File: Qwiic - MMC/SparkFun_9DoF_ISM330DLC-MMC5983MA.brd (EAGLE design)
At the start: 25.4 x 25.4 mm, 69 parts, among them J1 QWIIC_RIGHT_ANGLE, J2 QWIIC_RIGHT_ANGLE, U1 ISM330DLC, U2 MMC5983MA_QFN16

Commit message: Updates silk on board to reflect part change
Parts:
- removed U$31: (no value), top:ISM330DHCX5984
- added U$12: (no value), top:ISM330DLC5984
- U$10: device top:#ACC_SCL#8 -> top:#AUX_SCL#8
- U$11: device top:#ACC_SDA#7 -> top:#AUX_SDA#7
- U$23: device top:ISM330DHCX5984 -> top:ISM330DLC5984
- moved U$23 7.37 mm to (5.71, 13.0), flipped to the bottom, turned to 270 degrees
- moved U$11 0.13 mm to (16.5, 19.7)
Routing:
- net GND: vias 25 -> 24
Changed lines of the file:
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@@
 <attribute name="VALUE" x="8.89" y="17.018" size="0.6096" layer="27" font="vector" ratio="20" rot="R270" align="top-center"/>
 </element>
-<element name="U$10" library="top" package="#ACC_SCL#8" value="" x="13.97" y="19.812" smashed="yes" rot="MR270"/>
-<element name="U$11" library="top" package="#ACC_SDA#7" value="" x="16.637" y="19.685" smashed="yes" rot="MR270"/>
 <element name="U$19" library="top" package="#ASDA#9" value="" x="16.637" y="20.955" smashed="yes" rot="R90"/>
 <element name="U$20" library="top" package="#ASCL#10" value="" x="13.97" y="21.336" smashed="yes" rot="R90"/>
 <element name="U$21" library="top" package="MMC5983MA24" value="" x="6.985" y="20.32" smashed="yes" rot="R90"/>
-<element name="U$23" library="top" package="ISM330DHCX5984" value="" x="5.588" y="20.32" smashed="yes" rot="R90"/>
 <element name="U$24" library="top" package="9DOF24" value="" x="3.81" y="18.669" smashed="yes" rot="R90"/>
 <element name="U$30" library="top" package="9DOF24" value="" x="4.191" y="12.954" smashed="yes" rot="MR270"/>
-<element name="U$31" library="top" package="ISM330DHCX5984" value="" x="5.715" y="12.954" smashed="yes" rot="MR270"/>
 <element name="U$32" library="top" package="MMC5983MA24" value="" x="7.239" y="12.954" smashed="yes" rot="MR270"/>
 <element name="U$33" library="top" package="#0X6A#15" value="" x="22.987" y="7.239" smashed="yes" rot="MR0"/>
@@
 <element name="U$8" library="top" package="#MAG_INT#12" value="" x="8.89" y="19.812" smashed="yes" rot="MR270"/>
 <element name="U$9" library="top" package="#ACC_INT#11" value="" x="11.43" y="19.939" smashed="yes" rot="MR270"/>
+<element name="U$12" library="top" package="ISM330DLC5984" value="" x="5.461" y="19.812" smashed="yes" rot="R90"/>
+<element name="U$23" library="top" package="ISM330DLC5984" value="" x="5.715" y="12.954" smashed="yes" rot="MR270"/>
+<element name="U$10" library="top" package="#AUX_SCL#8" value="" x="13.97" y="19.812" smashed="yes" rot="MR270"/>
+<element name="U$11" library="top" package="#AUX_SDA#7" value="" x="16.51" y="19.685" smashed="yes" rot="MR270"/>
 </elements>
 <signals>
@@
 <via x="22.225" y="7.366" extent="1-16" drill="0.3048"/>
 <via x="6.604" y="14.224" extent="1-16" drill="0.3048"/>
-<via x="5.334" y="15.875" extent="1-16" drill="0.3048"/>
 <via x="19.3802" y="5.1308" extent="1-16" drill="0.3048"/>
 <via x="8.3058" y="7.1628" extent="1-16" drill="0.3048"/>
@@
 <via x="13.8938" y="5.8928" extent="1-16" drill="0.3048"/>
 <via x="14.6558" y="4.1148" extent="1-16" drill="0.3048"/>
-<wire x1="21.717" y1="19.685" x2="23.1775" y2="18.542" width="0" layer="19" extent="16-16"/>
-<wire x1="15.5702" y1="21.5138" x2="21.717" y2="19.685" width="0" layer="19" extent="1-1"/>
-<wire x1="14.1732" y1="21.6408" x2="15.5702" y2="21.5138" width="0" layer="19" extent="1-1"/>
-<wire x1="12.5222" y1="21.5138" x2="14.1732" y2="21.6408" width="0" layer="19" extent="1-1"/>
-<wire x1="10.795" y1="19.05" x2="12.5222" y2="21.5138" width="0" layer="19" extent="1-1"/>
-<wire x1="11.954" y1="15.385" x2="10.795" y2="19.05" width="0" layer="19" extent="1-1"/>
-<wire x1="12.954" y1="15.385" x2="11.954" y2="15.385" width="0" layer="19" extent="1-1"/>
-<wire x1="11.954" y1="14.328" x2="11.954" y2="15.385" width="0" layer="19" extent="1-1"/>
-<wire x1="10.287" y1="13.97" x2="11.596" y2="13.97" width="0" layer="19" extent="1-1"/>
-<wire x1="15.494" y1="14.263" x2="14.224" y2="14.732" width="0" layer="19" extent="1-1"/>
-<wire x1="15.494" y1="12.954" x2="15.494" y2="14.263" width="0" layer="19" extent="1-1"/>
-<wire x1="11.596" y1="12.446" x2="11.596" y2="13.97" width="0" layer="19" extent="1-1"/>
-<wire x1="10.287" y1="12.446" x2="11.596" y2="12.446" width="0" layer="19" extent="1-1"/>
-<wire x1="12.2" y1="10.906" x2="11.596" y2="12.446" width="0" layer="19" extent="1-1"/>
-<wire x1="12.7" y1="10.906" x2="12.2" y2="10.906" width="0" layer="19" extent="1-1"/>
-<wire x1="10.668" y1="8.509" x2="12.2" y2="10.906" width="0" layer="19" extent="1-1"/>
-<wire x1="9.652" y1="9.04965" x2="10.668" y2="8.509" width="0" layer="19" extent="1-1"/>
-<wire x1="8.3058" y1="7.1628" x2="9.652" y2="9.04965" width="0" layer="19" extent="1-1"/>
-<wire x1="7.7978" y1="5.8928" x2="8.3058" y2="7.1628" width="0" layer="19" extent="1-1"/>
-<wire x1="9.7536" y1="6.096" x2="8.3058" y2="7.1628" width="0" layer="19" extent="1-1"/>
-<wire x1="6.5278" y1="8.1788" x2="8.3058" y2="7.1628" width="0" layer="19" extent="1-1"/>
-<wire x1="10.4648" y1="2.9718" x2="9.7536" y2="6.096" width="0" layer="19" extent="1-1"/>
-<wire x1="12.2682" y1="2.5908" x2="10.4648" y2="2.9718" width="0" layer="19" extent="1-1"/>
-<wire x1="14.6558" y1="4.1148" x2="12.2682" y2="2.5908" width="0" layer="19" extent="1-1"/>
-<wire x1="13.8938" y1="5.8928" x2="14.6558" y2="4.1148" width="0" layer="19" extent="1-1"/>
-<wire x1="17.4752" y1="5.6388" x2="14.6558" y2="4.1148" width="0" layer="19" extent="1-1"/>
-<wire x1="19.3802" y1="5.1308" x2="17.4752" y2="5.6388" width="0" layer="19" extent="1-1"/>
-<wire x1="20.916" y1="7.366" x2="19.3802" y2="5.1308" width="0" layer="19" extent="1-1"/>
-<wire x1="22.225" y1="7.366" x2="20.916" y2="7.366" width="0" layer="19" extent="1-1"/>
-<wire x1="16.7132" y1="8.4328" x2="17.4752" y2="5.6388" width="0" layer="19" extent="1-1"/>
-<wire x1="20.447" y1="10.287" x2="20.916" y2="7.366" width="0" layer="19" extent="1-1"/>
-<wire x1="20.2946" y1="11.2" x2="20.447" y2="10.287" width="0" layer="19" extent="1-1"/>
-<wire x1="18.923" y1="11.176" x2="20.2946" y2="11.2" width="0" layer="19" extent="1-1"/>
-<wire x1="6.604" y1="14.224" x2="10.287" y2="13.97" width="0" layer="19" extent="1-1"/>
-<wire x1="5.08" y1="14.2" x2="6.604" y2="14.224" width="0" layer="19" extent="1-1"/>
-<wire x1="5.334" y1="15.875" x2="5.08" y2="14.2" width="0" layer="19" extent="1-1"/>
-<wire x1="6.35" y1="1.27" x2="10.4648" y2="2.9718" width="0" layer="19" extent="1-1"/>
 </signal>
 <signal name="SCL">
@@
 <wire x1="7.874" y1="11.811" x2="7.6835" y2="12.0015" width="0.4064" layer="1"/>
 <wire x1="7.6835" y1="12.0015" x2="7.6835" y2="12.7635" width="0.4064" layer="1"/>
-<wire x1="12.6116" y1="19.304" x2="12.954" y2="18.389" width="0" layer="19" extent="1-1"/>
-<wire x1="9.652" y1="10.74965" x2="9.779" y2="11.811" width="0" layer="19" extent="1-1"/>
-<wire x1="14.196" y1="16.127" x2="15.494" y2="15.963" width="0" layer="19" extent="1-1"/>
-<wire x1="8.1788" y1="10.74965" x2="9.652" y2="10.74965" width="0" layer="19" extent="1-1"/>
-<wire x1="13.2" y1="10.906" x2="13.296" y2="12.446" width="0" layer="19" extent="1-1"/>
-<wire x1="11.5375" y1="10.656" x2="13.2" y2="10.906" width="0" layer="19" extent="1-1"/>
 </signal>
 <signal name="N$5">

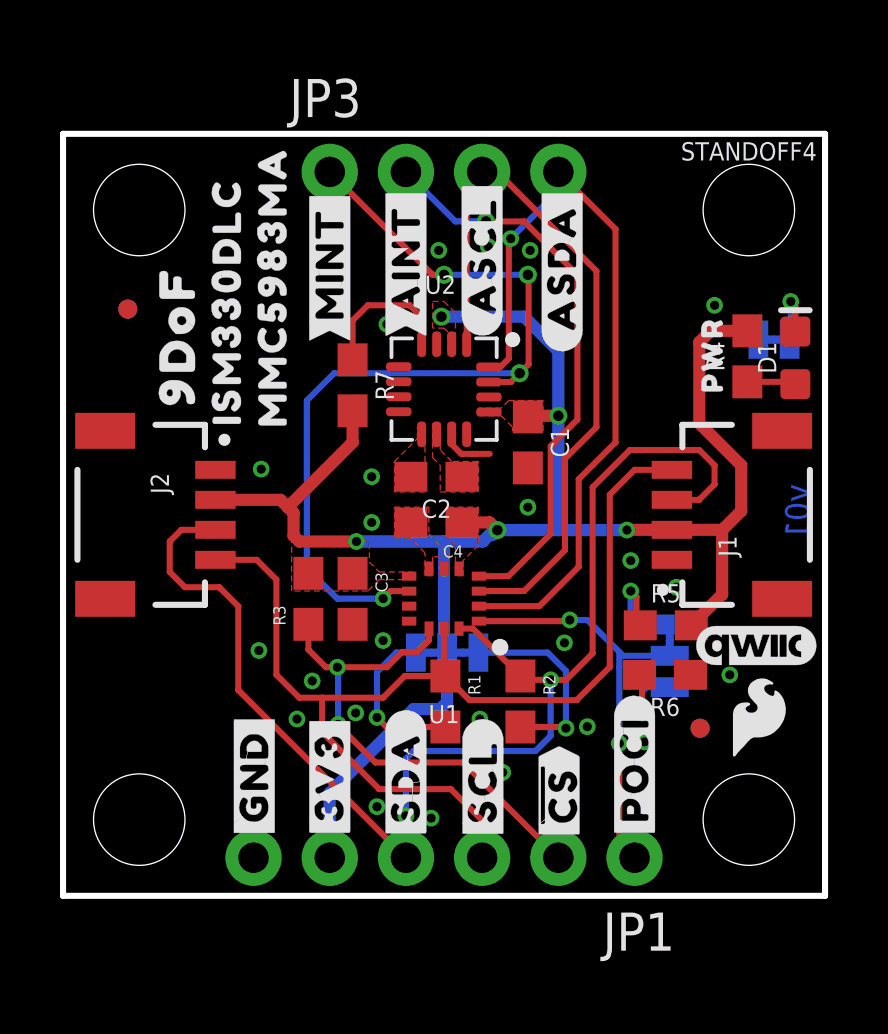
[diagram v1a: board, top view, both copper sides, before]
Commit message: Fixes clearance issue
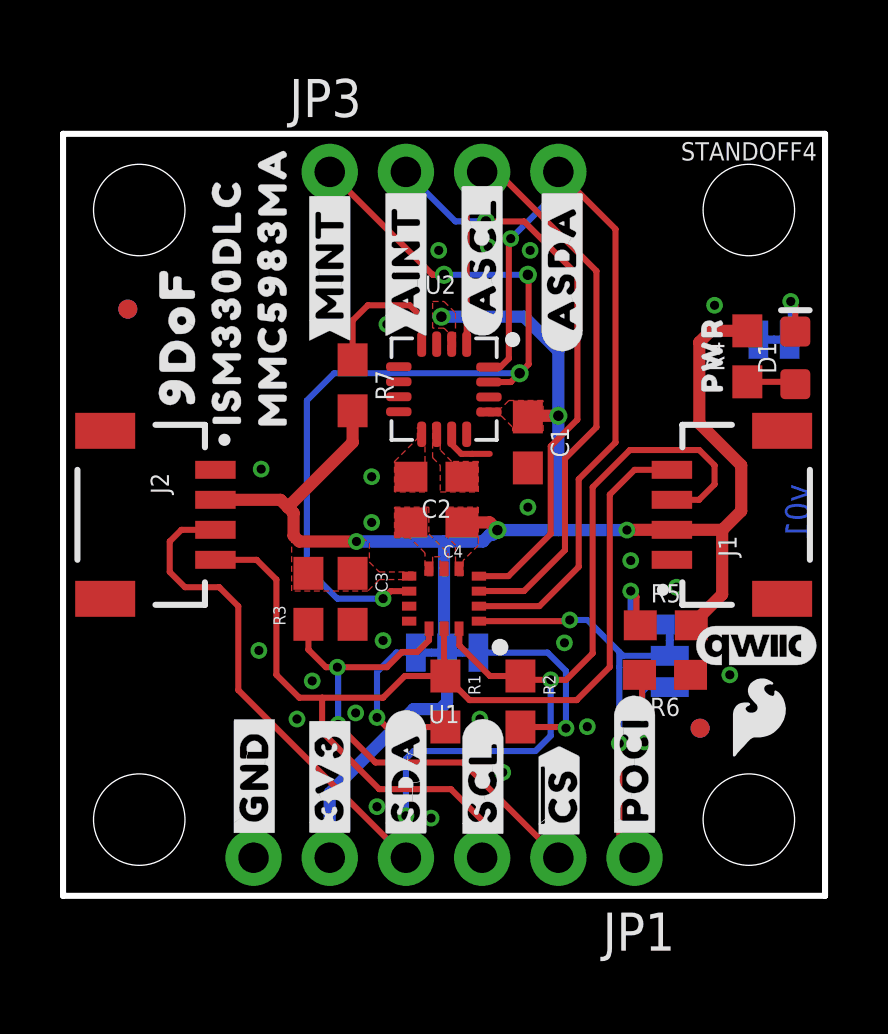
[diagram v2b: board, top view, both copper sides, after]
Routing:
- net GND: track 2.25 -> 1.74 mm
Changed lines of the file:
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@@
 <setting verticaltext="up"/>
 </settings>
-<grid distance="0.05" unitdist="inch" unit="inch" style="dots" multiple="1" display="yes" altdistance="0.005" altunitdist="inch" altunit="inch"/>
+<grid distance="0.05" unitdist="inch" unit="inch" style="dots" multiple="1" display="yes" altdistance="0.002" altunitdist="inch" altunit="inch"/>
 <layers>
 <layer number="1" name="Top" color="4" fill="1" visible="yes" active="yes"/>
@@
 <layer number="37" name="tTest" color="7" fill="1" visible="no" active="yes"/>
 <layer number="38" name="bTest" color="7" fill="1" visible="no" active="yes"/>
-<layer number="39" name="tKeepout" color="4" fill="11" visible="no" active="yes"/>
+<layer number="39" name="tKeepout" color="4" fill="11" visible="yes" active="yes"/>
 <layer number="40" name="bKeepout" color="1" fill="11" visible="no" active="yes"/>
 <layer number="41" name="tRestrict" color="4" fill="10" visible="no" active="yes"/>
@@
 <via x="10.287" y="13.97" extent="1-16" drill="0.3048"/>
 <via x="15.494" y="12.954" extent="1-16" drill="0.3048"/>
-<wire x1="11.954" y1="14.328" x2="11.596" y2="13.97" width="0.2032" layer="1"/>
 <wire x1="12.954" y1="15.385" x2="12.9484" y2="15.3794" width="0.2032" layer="1"/>
 <wire x1="12.9484" y1="15.3794" x2="12.9484" y2="15.0582125" width="0.2032" layer="1"/>
@@
 <contactref element="J2" pad="3"/>
 <contactref element="U1" pad="P14"/>
-<wire x1="15.24635" y1="7.327" x2="13.66735" y2="8.906" width="0.2032" layer="1"/>
-<wire x1="13.2" y1="8.906" x2="13.66735" y2="8.906" width="0.2032" layer="1"/>
+<wire x1="15.24635" y1="7.327" x2="14.23035" y2="7.327" width="0.2032" layer="1"/>
+<wire x1="14.23035" y1="7.327" x2="13.21015" y2="8.3472" width="0.2032" layer="1"/>
+<wire x1="13.2" y1="8.906" x2="13.21015" y2="8.89585" width="0.2032" layer="1"/>
+<wire x1="13.21015" y1="8.89585" x2="13.21015" y2="8.3472" width="0.2032" layer="1"/>
 <wire x1="16.77035" y1="7.2" x2="16.256" y2="7.2" width="0.2032" layer="1"/>
 <wire x1="16.256" y1="7.2" x2="15.37335" y2="7.2" width="0.2032" layer="1"/>
